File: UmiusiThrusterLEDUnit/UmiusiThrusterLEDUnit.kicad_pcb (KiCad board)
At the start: 2 copper layers, 56.3 x 58 mm, 9 parts, among them J1 Conn_01x04

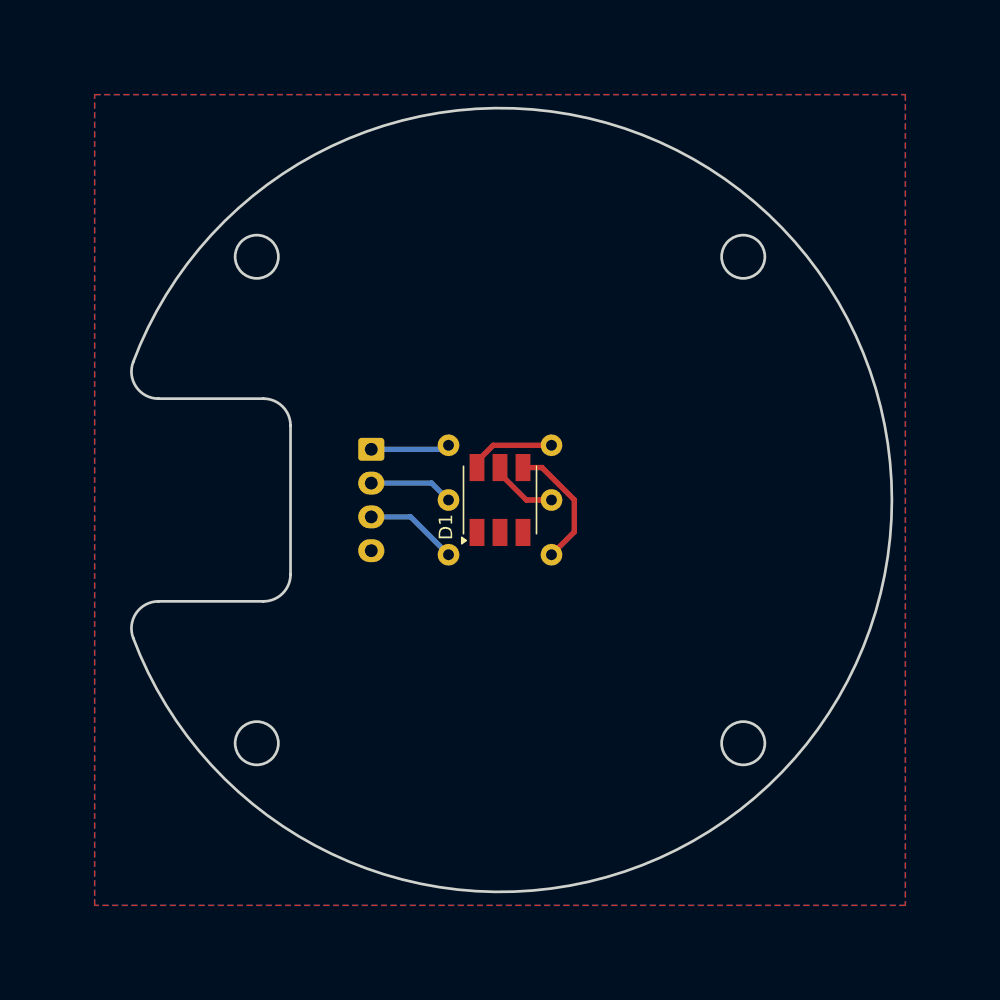
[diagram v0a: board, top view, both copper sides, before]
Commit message: スラスターLED用基板を修正
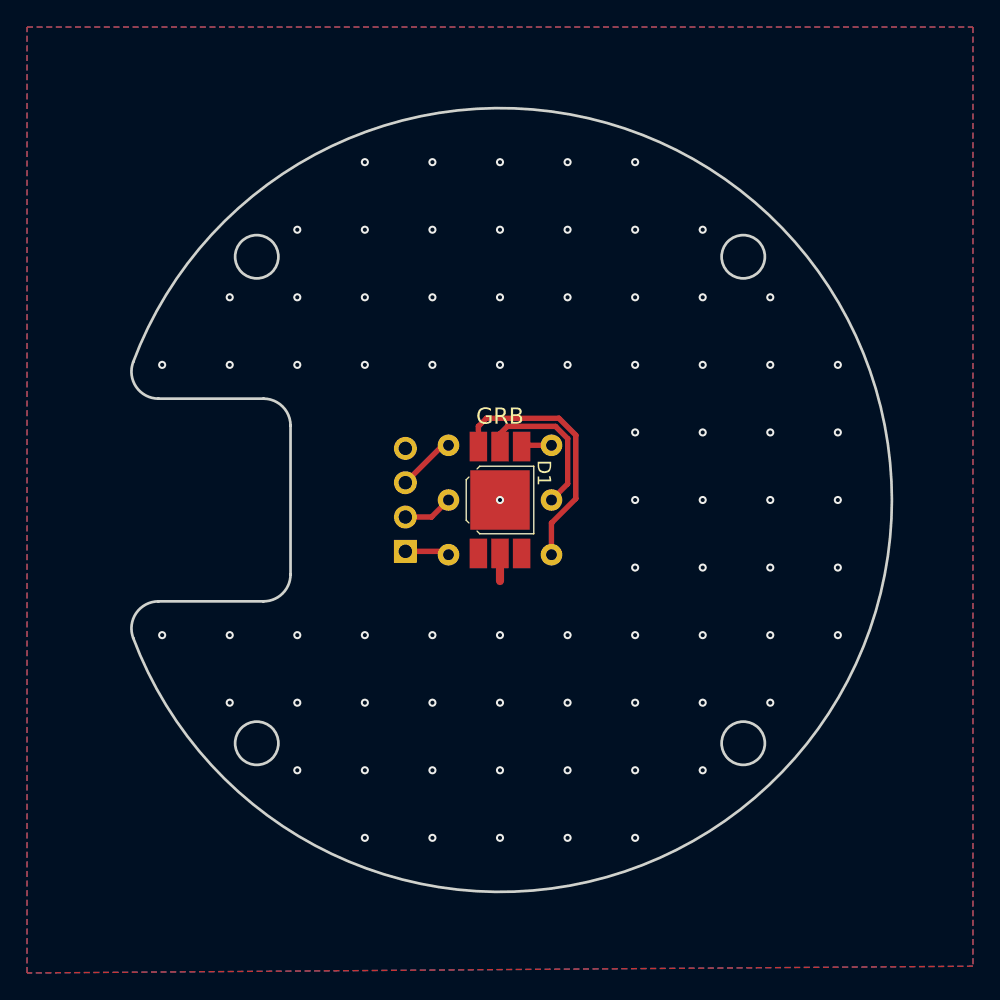
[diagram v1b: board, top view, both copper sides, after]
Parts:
- added G***: LOGO, aqua_logo:aqua_logo, B.Cu at (100.0, 111.5)
- D1: value LED_RGB -> OSTCXBTHC1E; footprint LED_SMD:LED_RGB_5050-6 -> PowerLED:OSTCXBTHC1E
- J1: footprint Connector_JST:JST_XH_B4B-XH-A_1x04_P2.50mm_Vertical -> Connector_PinHeader_2.54mm:PinHeader_1x04_P2.54mm_Vertical
- moved R1 8.10 mm to (103.8, 104.0)
- moved R3 8.10 mm to (103.8, 96.0)
- moved J1 7.96 mm to (93.0, 103.8), turned to 0 degrees
- turned D1 to -90 degrees
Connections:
- D1 pad 1: GND -> Net-(D1-GA)
- D1 pad 2: GND -> Net-(D1-RA)
- D1 pad 3: GND -> Net-(D1-BA)
- D1 pad 4: Net-(D1-BA) -> GND
- D1 pad 5: Net-(D1-GA) -> GND
- D1 pad 6: Net-(D1-RA) -> GND
- R1 pad 1: Net-(D1-RA) -> Net-(D1-GA)
- R2 pad 1: Net-(D1-GA) -> Net-(D1-RA)
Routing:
- net Net-(D1-GA): track 5.07 -> 19.1 mm
- net Net-(D1-BA): track 9.55 -> 2.29 mm
- net Net-(D1-RA): track 6.46 -> 11.6 mm
- net G_LED: track 5.84 -> 3.29 mm
- net R_LED: track 6.23 -> 3.71 mm
- net B_LED: track 6.87 -> 4.76 mm
- net GND: track 0.00 -> 2.05 mm, vias 0 -> 77
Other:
- board text added: "B R G"
- board text added: "GRB"
- board text added: "REV01"
- board text added: "Thruster LED Unit"

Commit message: modified
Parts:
- moved D1 56.6 mm to (58.0, 62.0)
- moved G*** 56.6 mm to (58.0, 73.5)
- moved J1 56.6 mm to (51.0, 65.8)
- moved R1 56.6 mm to (61.8, 66.0)
- moved R2 56.6 mm to (61.8, 62.0)
- moved R3 56.6 mm to (61.8, 58.0)
- moved REF** 56.6 mm to (40.0, 80.0)
- moved REF** 56.6 mm to (76.0, 44.0)
- moved REF** 56.6 mm to (76.0, 80.0)
- moved REF** 56.6 mm to (40.0, 44.0)
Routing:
- net GND: vias 77 -> 80

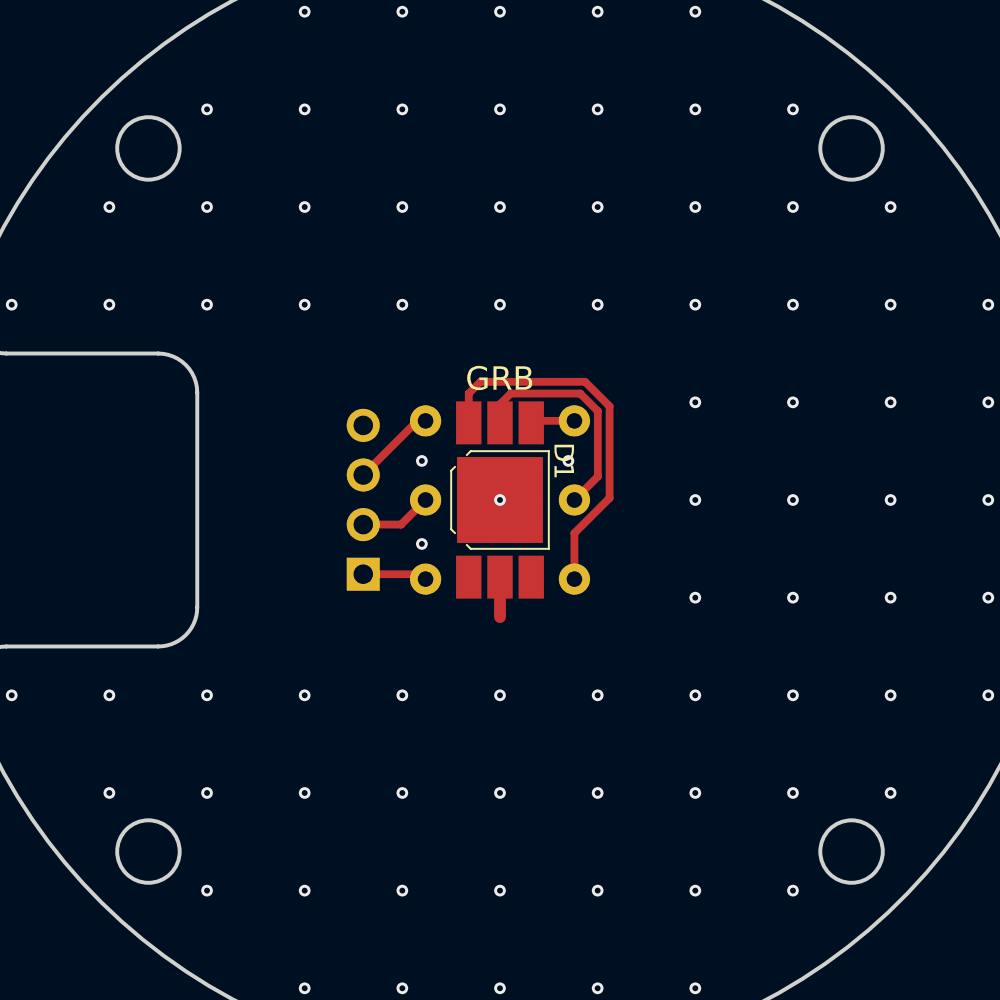
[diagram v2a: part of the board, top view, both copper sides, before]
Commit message: スラスタLED基盤　REV02作成
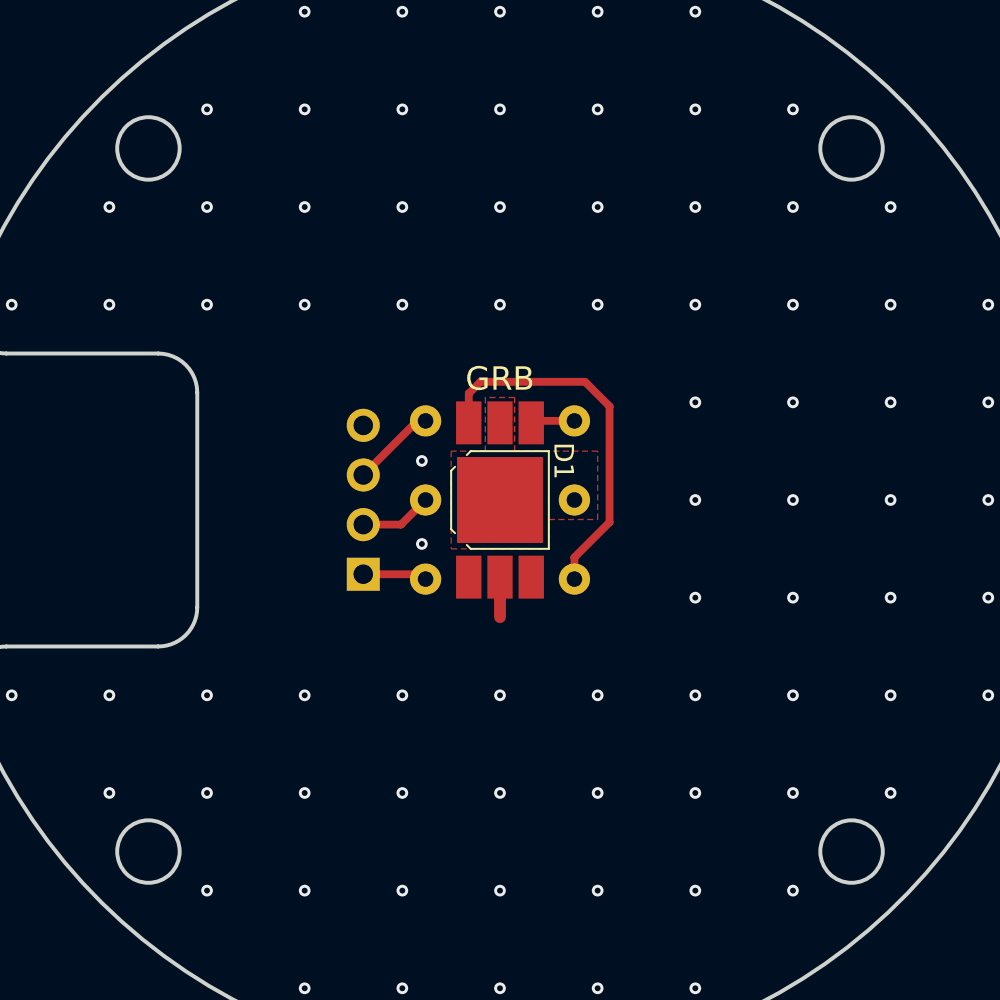
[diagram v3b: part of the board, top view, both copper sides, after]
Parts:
- removed REF** (x4): MountingHole_3.2mm_M3, MountingHole:MountingHole_3.2mm_M3
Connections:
- D1 pad 2: Net-(D1-RA) -> Net-(D1-PAD)
- D1 pad 7: GND -> Net-(D1-PAD)
- R2 pad 1: Net-(D1-RA) -> Net-(D1-PAD)
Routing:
- net Net-(D1-RA): track 11.6 -> 0.00 mm
- net GND: vias 80 -> 78
- added copper zone on F.Cu, net Net-(D1-PAD)
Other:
- board text added: "REV02"
- board text removed: "REV01"
